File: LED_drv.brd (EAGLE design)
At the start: 160 x 100 mm, 42 parts, among them IC1 LM3409, IC2 LM393D, T1 IRLR9343PBF, T4 BT169, T5 BT169, T6 TLP266J

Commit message: Charge regeneration circuit
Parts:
- added C7: 1u/50V, rcl:C1206
- added D4: 5V1, diode:SOD80C
- added D6: 36V, diode:SOD80C
- added R22: 330R, resistor:R0805
- R10: value 33k -> 150k
- R11, R8, R9: value 33k -> 100k
- R12: value 33k -> 47k
- R13: value 33k -> 15k
- moved R13 305.7 mm to (-72.4, -251.5)
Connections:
- removed net V+: IC2.8
- removed net V-: IC2.4
- new net N$19: C7.1, D6.C, IC2.8, R13.1, R22.2
- new net N$20: IC2.3, R10.1, R11.1
- new net N$21: IC2.2, R8.2, R9.1
- new net N$22: D4.C, R11.2, R12.2
- new net N$27: R12.1, R22.1, R8.1
- new net N$29: IC2.1, R10.2, R13.2
- net GND: now also C7.2, D4.A, D6.A, IC2.4, IC2.5, IC2.6, IC2.7, R9.2
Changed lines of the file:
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@@
 <element name="L1" library="miscrel" package="CDRH104-R" value="CDRH104R" x="-36.83" y="8.89"/>
 <element name="R1" library="rcl" package="R0805" value="" x="-52.07" y="49.53"/>
-<element name="R10" library="resistor" package="R0805" value="33k" x="-54.61" y="44.45"/>
-<element name="R11" library="resistor" package="R0805" value="33k" x="-16.51" y="50.8"/>
-<element name="R12" library="resistor" package="R0805" value="33k" x="-21.59" y="50.8"/>
-<element name="R13" library="resistor" package="R0805" value="33k" x="-26.67" y="50.8"/>
+<element name="R10" library="resistor" package="R0805" value="150k" x="-54.61" y="44.45"/>
+<element name="R11" library="resistor" package="R0805" value="100k" x="-16.51" y="50.8"/>
+<element name="R12" library="resistor" package="R0805" value="47k" x="-21.59" y="50.8"/>
 <element name="R2" library="rcl" package="R0805" value="" x="-15.24" y="55.88"/>
 <element name="R3" library="rcl" package="R0805" value="1k" x="-46.99" y="50.8"/>
@@
 <element name="R6" library="pot" package="3RP/1610N" value="470k" x="-21.59" y="13.97"/>
 <element name="R7" library="rcl" package="R0805" value="15k" x="-31.75" y="50.8"/>
-<element name="R8" library="resistor" package="R0805" value="33k" x="-36.83" y="50.8"/>
-<element name="R9" library="resistor" package="R0805" value="33k" x="-41.91" y="50.8"/>
+<element name="R8" library="resistor" package="R0805" value="100k" x="-36.83" y="50.8"/>
+<element name="R9" library="resistor" package="R0805" value="100k" x="-41.91" y="50.8"/>
 <element name="S1" library="switch-omron" package="SW_DUMMY" value="SW_DUMMY" x="-20.32" y="55.88"/>
 <element name="T1" library="miscrel" package="TO252-3-11" value="IRLR9343PBF" x="-48.26" y="6.35"/>
@@
 <element name="R18" library="rcl" package="R1206" value="700R" x="-71.12" y="-212.09"/>
 <element name="C8" library="rcl" package="E3,5-8" value="100u" x="-69.85" y="-219.71"/>
+<element name="D4" library="diode" package="SOD80C" value="5V1" x="-71.12" y="-227.33"/>
+<element name="D6" library="diode" package="SOD80C" value="36V" x="-71.12" y="-232.41"/>
+<element name="R22" library="resistor" package="R0805" value="330R" x="-72.39" y="-237.49"/>
+<element name="C7" library="rcl" package="C1206" value="1u/50V" x="-69.85" y="-245.11"/>
+<element name="R13" library="resistor" package="R0805" value="15k" x="-72.39" y="-251.46"/>
 </elements>
 <signals>
-<signal name="V+">
-<contactref element="IC2" pad="8"/>
-</signal>
-<signal name="V-">
-<contactref element="IC2" pad="4"/>
-</signal>
 <signal name="N$1">
 <contactref element="R1" pad="2"/>
@@
 <contactref element="R6" pad="1"/>
 <contactref element="C5" pad="2"/>
-<wire x1="-21.59" y1="36.83" x2="-18.92" y2="44.45" width="0" layer="19" extent="1-1"/>
-<wire x1="-31.43" y1="44.45" x2="-21.59" y2="36.83" width="0" layer="19" extent="1-1"/>
-<wire x1="-36.83" y1="36.83" x2="-31.43" y2="44.45" width="0" layer="19" extent="1-1"/>
+<contactref element="R9" pad="2"/>
+<contactref element="IC2" pad="4"/>
+<contactref element="D4" pad="A"/>
+<contactref element="D6" pad="A"/>
+<contactref element="C7" pad="2"/>
+<contactref element="IC2" pad="6"/>
+<contactref element="IC2" pad="7"/>
+<contactref element="IC2" pad="5"/>
+<wire x1="-69.42" y1="-232.41" x2="-68.45" y2="-245.11" width="0" layer="19" extent="1-1"/>
+<wire x1="-69.42" y1="-227.33" x2="-69.42" y2="-232.41" width="0" layer="19" extent="1-1"/>
+<wire x1="-26.59" y1="13.97" x2="-69.42" y2="-227.33" width="0" layer="19" extent="1-1"/>
+<wire x1="-29.48" y1="24.27" x2="-26.59" y2="13.97" width="0" layer="19" extent="1-1"/>
+<wire x1="-30.48" y1="26.67" x2="-29.48" y2="24.27" width="0" layer="19" extent="1-1"/>
+<wire x1="-36.83" y1="36.83" x2="-30.48" y2="26.67" width="0" layer="19" extent="1-1"/>
 <wire x1="-44.94" y1="35.56" x2="-36.83" y2="36.83" width="0" layer="19" extent="1-1"/>
-<wire x1="-30.48" y1="26.67" x2="-36.83" y2="36.83" width="0" layer="19" extent="1-1"/>
-<wire x1="-29.48" y1="24.27" x2="-30.48" y2="26.67" width="0" layer="19" extent="1-1"/>
-<wire x1="-26.59" y1="13.97" x2="-29.48" y2="24.27" width="0" layer="19" extent="1-1"/>
-<wire x1="-53.02" y1="49.53" x2="-44.94" y2="35.56" width="0" layer="19" extent="1-1"/>
+<wire x1="-46.355" y1="28" x2="-44.94" y2="35.56" width="0" layer="19" extent="1-1"/>
+<wire x1="-47.625" y1="28" x2="-46.355" y2="28" width="0" layer="19" extent="1-1"/>
+<wire x1="-48.895" y1="28" x2="-47.625" y2="28" width="0" layer="19" extent="1-1"/>
+<wire x1="-46.355" y1="22.8" x2="-46.355" y2="28" width="0" layer="19" extent="1-1"/>
+<wire x1="-31.43" y1="44.45" x2="-36.83" y2="36.83" width="0" layer="19" extent="1-1"/>
+<wire x1="-40.96" y1="50.8" x2="-31.43" y2="44.45" width="0" layer="19" extent="1-1"/>
+<wire x1="-53.02" y1="49.53" x2="-40.96" y2="50.8" width="0" layer="19" extent="1-1"/>
+<wire x1="-21.59" y1="36.83" x2="-31.43" y2="44.45" width="0" layer="19" extent="1-1"/>
+<wire x1="-18.92" y1="44.45" x2="-21.59" y2="36.83" width="0" layer="19" extent="1-1"/>
 </signal>
 <signal name="N$4">
@@
 <wire x1="-70.77" y1="-197.62" x2="-69.698" y2="-212.09" width="0" layer="19" extent="1-1"/>
 </signal>
+<signal name="N$20">
+<contactref element="R10" pad="1"/>
+<contactref element="R11" pad="1"/>
+<contactref element="IC2" pad="3"/>
+<wire x1="-55.56" y1="44.45" x2="-17.46" y2="50.8" width="0" layer="19" extent="1-1"/>
+<wire x1="-47.625" y1="22.8" x2="-55.56" y2="44.45" width="0" layer="19" extent="1-1"/>
+</signal>
+<signal name="N$21">
+<contactref element="R8" pad="2"/>
+<contactref element="R9" pad="1"/>
+<contactref element="IC2" pad="2"/>
+<wire x1="-42.86" y1="50.8" x2="-48.895" y2="22.8" width="0" layer="19" extent="1-1"/>
+<wire x1="-35.88" y1="50.8" x2="-42.86" y2="50.8" width="0" layer="19" extent="1-1"/>
+</signal>
+<signal name="N$22">
+<contactref element="R11" pad="2"/>
+<contactref element="R12" pad="2"/>
+<contactref element="D4" pad="C"/>
+<wire x1="-20.64" y1="50.8" x2="-72.82" y2="-227.33" width="0" layer="19" extent="1-1"/>
+<wire x1="-15.56" y1="50.8" x2="-20.64" y2="50.8" width="0" layer="19" extent="1-1"/>
+</signal>
+<signal name="N$27">
+<contactref element="R12" pad="1"/>
+<contactref element="R8" pad="1"/>
+<contactref element="R22" pad="1"/>
+<wire x1="-37.78" y1="50.8" x2="-73.34" y2="-237.49" width="0" layer="19" extent="1-1"/>
+<wire x1="-22.54" y1="50.8" x2="-37.78" y2="50.8" width="0" layer="19" extent="1-1"/>
+</signal>
+<signal name="N$29">
+<contactref element="R10" pad="2"/>
+<contactref element="IC2" pad="1"/>
+<contactref element="R13" pad="2"/>
+<wire x1="-50.165" y1="22.8" x2="-71.44" y2="-251.46" width="0" layer="19" extent="1-1"/>
+<wire x1="-53.66" y1="44.45" x2="-50.165" y2="22.8" width="0" layer="19" extent="1-1"/>
+</signal>
+<signal name="N$19">
+<contactref element="IC2" pad="8"/>
+<contactref element="D6" pad="C"/>
+<contactref element="R22" pad="2"/>
+<contactref element="C7" pad="1"/>
+<contactref element="R13" pad="1"/>
+<wire x1="-71.25" y1="-245.11" x2="-73.34" y2="-251.46" width="0" layer="19" extent="1-1"/>
+<wire x1="-71.44" y1="-237.49" x2="-71.25" y2="-245.11" width="0" layer="19" extent="1-1"/>
+<wire x1="-72.82" y1="-232.41" x2="-71.44" y2="-237.49" width="0" layer="19" extent="1-1"/>
+<wire x1="-50.165" y1="28" x2="-72.82" y2="-232.41" width="0" layer="19" extent="1-1"/>
+</signal>
 </signals>

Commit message: Analog circuitry & switch correction
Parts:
- added C9: 100uF/50V, rcl:E3,5-8
- added D12: 1n4007, diode:DO-214AC
- added Q2: IRF840, transistor-fet:TO220
- added R23: 8M2, resistor:R0805
- added R25: 390R, resistor:R0805
- added R29: 330R, rcl:R1206
- added R30: 1M, rcl:R1206
- added T2: BC847, transistor:SOT23
- D5: value 1n4007 -> 18V; device diode:DO-214AC -> diode:SOD80C
- R14: value 330R/200V -> 2M
- R16: value 1M/200V -> 2M
- R17: value 1M/200V -> 47R; device rcl:R1206 -> resistor:R0805
- moved R17 366.0 mm to (-86.4, -401.3)
- moved R14 118.1 mm to (-71.1, -270.5)
- moved D5 104.1 mm to (-71.1, -264.2)
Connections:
- removed net N$24: B1.AC1, D9.A, R15.1, T4.2, T5.3
- new net 5V1_ZEN: D4.C, R11.2, R12.2, T2.1
- new net N$28: IC2.7, R17.1
- new net N$30: IC2.5, R17.2, R23.1, R25.2
- new net N$38: Q2.2, R29.1
- new net N$39: D12.A, Q2.3
- new net NAH: B1.AC2, D3.A, R19.2, R29.2, T4.3, T5.2
- new net V+: C9.+, R12.1, R22.1, R8.1, T6.1
- net 230VAC(L/N): now also B1.AC1; no longer D3.A, R19.2, T4.3, T5.2
- net 230VAC(N/L): now also D5.A, D9.A, R15.1, R30.1, T4.2, T5.3; no longer B1.AC2, R17.2
- net GND: now also C9.-, R23.2; no longer IC2.5, IC2.6, IC2.7
- net N$12: no longer R14.1
- net N$15: now also R14.1, R16.2; no longer D5.A, R14.2
- net N$16: now also D12.C; no longer D5.C
- net N$22: now also R25.1, T2.2; no longer D4.C, R11.2, R12.2
- net N$27: now also T2.3, T6.3; no longer R12.1, R22.1, R8.1
- net N$29: now also IC2.6
- net N$7: now also D5.C, Q2.1, R14.2, R30.2; no longer R16.2, R17.1

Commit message: Additional corrections
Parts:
- added R24: 2M2, resistor:R0805
- R23: value 8M2 -> 2M2
- T2: value BC847 -> (none); device transistor:SOT23 -> transistor:SOT89-BCE
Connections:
- new net N$21: IC2.5, R23.1, R24.1
- net 5V1_ZEN: now also T2.B; no longer T2.1
- net N$22: now also T2.E; no longer T2.2
- net N$27: now also T2.C; no longer T2.3
- net N$30: now also R24.2; no longer IC2.5, R23.1
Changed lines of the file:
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@@
 <element name="Q2" library="transistor-fet" package="TO220" value="IRF840" x="-83.82" y="-322.58"/>
 <element name="D12" library="diode" package="DO-214AC" value="1n4007" x="-85.09" y="-336.55"/>
-<element name="R23" library="resistor" package="R0805" value="8M2" x="-86.36" y="-367.03"/>
-<element name="T2" library="transistor" package="SOT23" value="BC847" x="-86.36" y="-381"/>
+<element name="R23" library="resistor" package="R0805" value="2M2" x="-86.36" y="-367.03"/>
+<element name="T2" library="transistor" package="SOT89-BCE" value="" x="-86.36" y="-381"/>
 <element name="R25" library="resistor" package="R0805" value="390R" x="-86.36" y="-394.97"/>
 <element name="R17" library="resistor" package="R0805" value="47R" x="-86.36" y="-401.32"/>
 <element name="C9" library="rcl" package="E3,5-8" value="100uF/50V" x="-83.82" y="-408.94"/>
+<element name="R24" library="resistor" package="R0805" value="2M2" x="-86.36" y="-416.56"/>
 </elements>
 <signals>
@@
 <contactref element="R12" pad="2"/>
 <contactref element="D4" pad="C"/>
-<contactref element="T2" pad="1"/>
-<wire x1="-72.82" y1="-227.33" x2="-87.31" y2="-382.1" width="0" layer="19" extent="1-1"/>
+<contactref element="T2" pad="B"/>
+<wire x1="-72.82" y1="-227.33" x2="-87.859" y2="-382.981" width="0" layer="19" extent="1-1"/>
 <wire x1="-20.64" y1="50.8" x2="-72.82" y2="-227.33" width="0" layer="19" extent="1-1"/>
 <wire x1="-15.56" y1="50.8" x2="-20.64" y2="50.8" width="0" layer="19" extent="1-1"/>
@@
 </signal>
 <signal name="N$30">
-<contactref element="R23" pad="1"/>
-<contactref element="IC2" pad="5"/>
 <contactref element="R25" pad="2"/>
 <contactref element="R17" pad="2"/>
+<contactref element="R24" pad="2"/>
+<wire x1="-85.41" y1="-401.32" x2="-85.41" y2="-416.56" width="0" layer="19" extent="1-1"/>
 <wire x1="-85.41" y1="-394.97" x2="-85.41" y2="-401.32" width="0" layer="19" extent="1-1"/>
-<wire x1="-87.31" y1="-367.03" x2="-85.41" y2="-394.97" width="0" layer="19" extent="1-1"/>
-<wire x1="-46.355" y1="28" x2="-87.31" y2="-367.03" width="0" layer="19" extent="1-1"/>
 </signal>
 <signal name="N$22">
-<contactref element="T2" pad="2"/>
+<contactref element="T2" pad="E"/>
 <contactref element="R25" pad="1"/>
-<wire x1="-85.41" y1="-382.1" x2="-87.31" y2="-394.97" width="0" layer="19" extent="1-1"/>
+<wire x1="-84.861" y1="-382.981" x2="-87.31" y2="-394.97" width="0" layer="19" extent="1-1"/>
 </signal>
 <signal name="N$27">
 <contactref element="T6" pad="3"/>
-<contactref element="T2" pad="3"/>
-<wire x1="-73" y1="-85.09" x2="-86.36" y2="-379.9" width="0" layer="19" extent="1-1"/>
+<contactref element="T2" pad="C"/>
+<wire x1="-73" y1="-85.09" x2="-86.36" y2="-382.727" width="0" layer="19" extent="1-1"/>
 </signal>
 <signal name="N$28">
@@
 <wire x1="-35.88" y1="50.8" x2="-42.86" y2="50.8" width="0" layer="19" extent="1-1"/>
 </signal>
+<signal name="N$21">
+<contactref element="R23" pad="1"/>
+<contactref element="IC2" pad="5"/>
+<contactref element="R24" pad="1"/>
+<wire x1="-87.31" y1="-367.03" x2="-87.31" y2="-416.56" width="0" layer="19" extent="1-1"/>
+<wire x1="-46.355" y1="28" x2="-87.31" y2="-367.03" width="0" layer="19" extent="1-1"/>
+</signal>
 </signals>

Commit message: Mains side PCB layout
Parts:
- removed B1: (no value), rectifier:FBP1,5
- removed C8: 100u, rcl:E3,5-8
- removed D12: 1n4007, diode:DO-214AC
- added D7: 1n4007, diode:DO-214AC
- added D8: 10V, diode:SOD80C
- added PAD1, PAD2, PAD3, PAD4: (no value), wirepad:SMD2,54-5,08
- added R26: 10M, rcl:R1206
- Q2: value IRF840 -> IPD50R380; device transistor-fet:TO220 -> miscrel:TO252-3-11
- R18: value 700R -> 10M
- T2: value (none) -> BCX56; device transistor:SOT89-BCE -> miscrel:SOT89
- moved R25 479.5 mm to (-20.3, 80.0)
- moved C9 475.8 mm to (-39.4, 64.8)
- moved T2 453.3 mm to (-11.4, 66.0)
- moved R24 446.6 mm to (-14.0, 24.1)
- moved R17 436.4 mm to (-15.2, 29.2)
- moved R23 394.0 mm to (-7.62, 19.1)
- moved R29 392.9 mm to (62.2, 47.0), turned to 90 degrees
- moved Q2 390.3 mm to (55.9, 41.9), turned to 90 degrees
- moved R30 387.0 mm to (64.1, 33.7), turned to 90 degrees
- moved R14 336.4 mm to (62.9, 38.1), turned to 180 degrees
- moved D5 326.0 mm to (61.6, 33.7), turned to 270 degrees
- moved R18 290.5 mm to (72.5, 40.4), turned to 180 degrees
- moved R13 288.2 mm to (-12.7, 30.5)
- moved D4 275.8 mm to (-11.4, 41.9)
- moved D6 274.3 mm to (-12.7, 35.6)
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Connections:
- removed net N$17: B1.+, C8.+, R18.1
- removed net N$18: B1.-, C8.-, R18.2
- new net N$24: D7.C, R29.2
- new net N$33: D8.C, Q2.3
- net 230VAC(L/N): now also PAD1.1, PAD4.1; no longer B1.AC1
- net 230VAC(N/L): now also PAD2.1, R26.2, T4.4
- net N$14: now also R18.1
- net N$16: now also R21.2, T6.4; no longer D12.C, D9.C, R15.2, R21.1, T5.1
- net N$25: now also R20.2; no longer R21.2
- net N$26: now also R18.2, R26.1; no longer R20.2, T6.4
- net N$27: now also T2.C@1
- net N$39: now also D8.A, D9.C, R15.2, R21.1, T5.1; no longer D12.A, Q2.3
- net NAH: now also D7.A, PAD3.1, T5.4; no longer B1.AC2, R29.2
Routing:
- net 230VAC(N/L): track 0.00 -> 76.3 mm
- net NAH: track 0.00 -> 47.4 mm
- net N$39: track 0.00 -> 16.6 mm
- net N$23: track 0.00 -> 15.0 mm
- net N$7: track 0.00 -> 7.31 mm
- net N$33: track 0.00 -> 5.82 mm
- net N$24: track 0.00 -> 3.50 mm
- net N$26: track 0.00 -> 3.35 mm
- net N$15: track 0.00 -> 3.06 mm
- net N$38: track 0.00 -> 2.81 mm
- net 230VAC(L/N): track 0.00 -> 2.79 mm
- net N$16: track 0.00 -> 1.99 mm
- net N$25: track 0.00 -> 1.78 mm

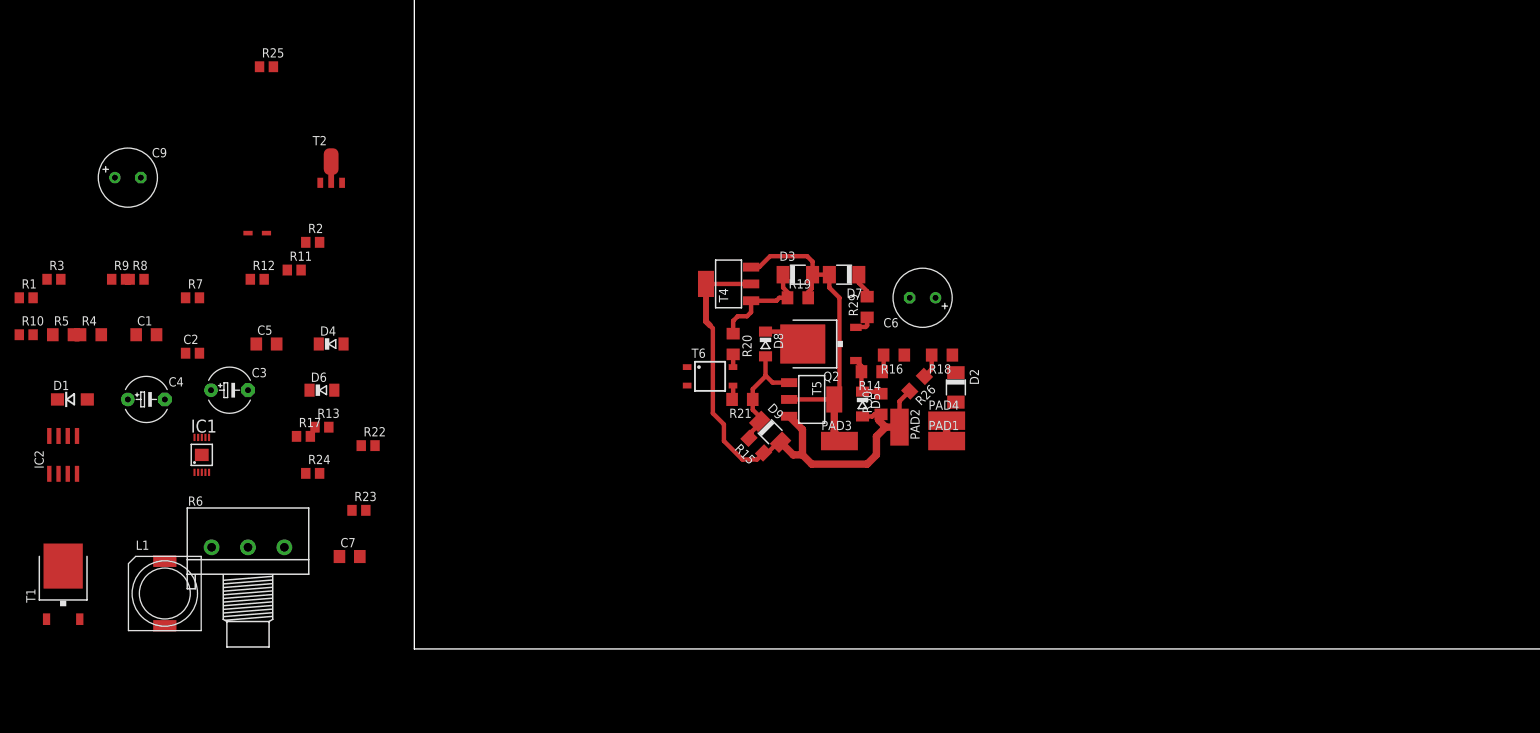
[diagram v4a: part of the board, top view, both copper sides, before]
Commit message: key side PCB layout
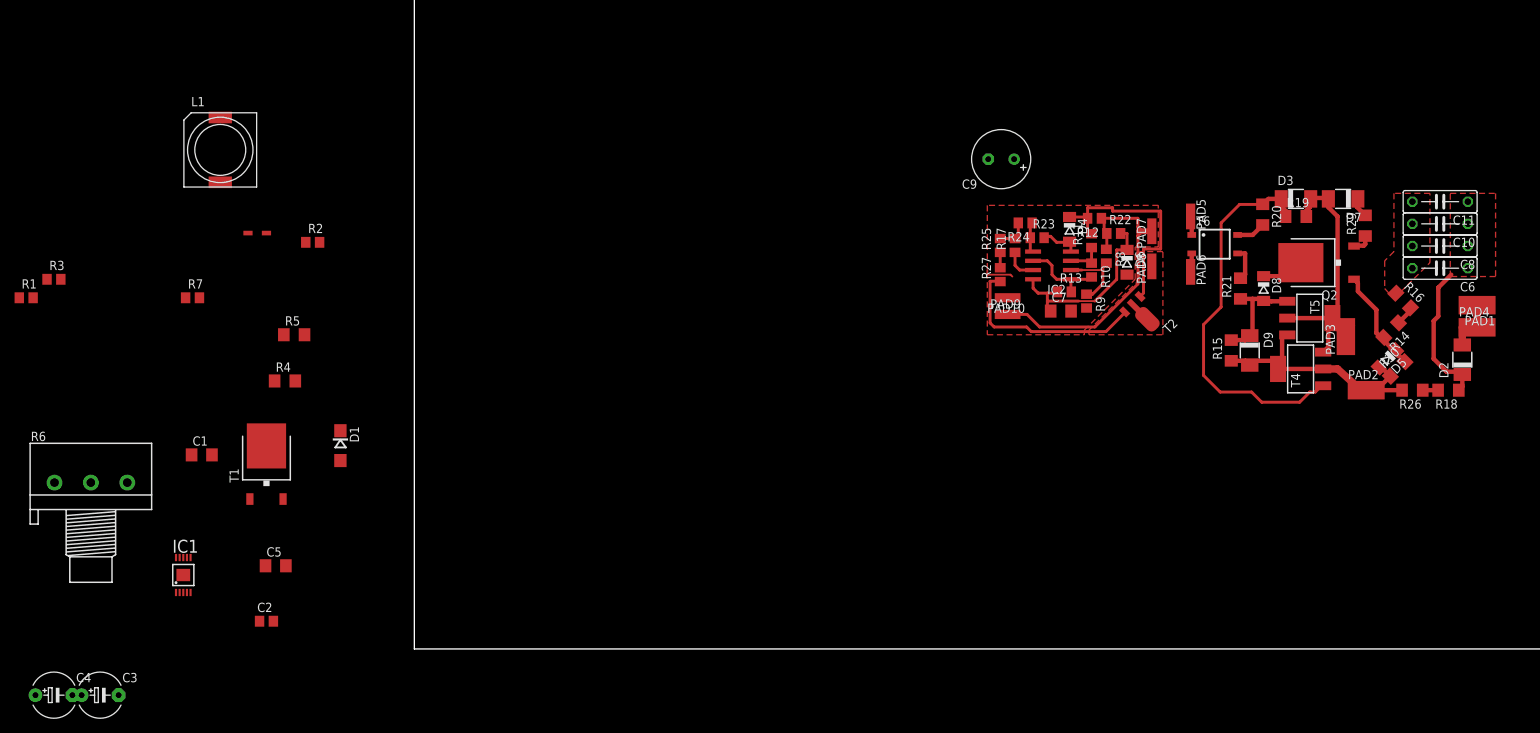
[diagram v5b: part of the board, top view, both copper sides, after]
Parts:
- added C10, C11, C8: 100n/400V, rcl:C075-032X103
- added PAD10, PAD5, PAD6, PAD7, PAD8, PAD9: (no value), wirepad:SMD1,27-2,54
- added R27: 0, resistor:R0805
- C6: device rcl:E3,5-8 -> rcl:C075-032X103
- moved R10 146.7 mm to (93.1, 52.1), turned to 270 degrees
- moved IC2 138.4 mm to (87.6, 52.7), turned to 90 degrees
- moved R8 133.2 mm to (95.1, 54.0), turned to 270 degrees
- moved R9 133.1 mm to (92.4, 47.8), turned to 270 degrees
- moved C9 120.0 mm to (80.6, 67.3), turned to 180 degrees
- moved R12 115.4 mm to (93.5, 59.2), turned to 180 degrees
- moved T2 113.3 mm to (100.1, 46.0), turned to 225 degrees
- moved D6 112.0 mm to (97.9, 53.1), turned to 270 degrees
- moved R11 109.6 mm to (93.1, 56.1), turned to 90 degrees
- moved R22 106.5 mm to (96.1, 57.1)
- moved R24 103.8 mm to (83.9, 58.5), turned to 180 degrees
- moved R25 103.8 mm to (80.5, 55.4), turned to 90 degrees
- moved R13 103.7 mm to (89.3, 49.1)
- moved C7 103.4 mm to (88.8, 46.4)
- moved D4 102.7 mm to (90.0, 57.7), turned to 270 degrees
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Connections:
- new net N$34: C10.2, C11.2, C6.2, C8.2, R16.1
- net GND: now also PAD10.1
- net N$12: now also R25.1, R27.2; no longer C6.-, R16.1
- net N$14: now also C10.1, C11.1, C6.1, C8.1; no longer C6.+
- net N$22: now also R27.1; no longer R25.1
- net N$27: now also PAD6.1, PAD8.1
- net V+: now also PAD5.1, PAD7.1, PAD9.1
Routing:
- net V+: track 0.00 -> 45.2 mm
- net 230VAC(N/L): track 76.3 -> 36.4 mm
- net N$23: track 15.0 -> 53.3 mm
- net 5V1_ZEN: track 0.00 -> 31.6 mm
- net N$22: track 0.00 -> 27.3 mm
- net N$31: track 0.00 -> 27.1 mm
- net N$14: track 0.00 -> 19.8 mm
- net N$29: track 0.00 -> 11.7 mm
- net N$19: track 0.00 -> 10.3 mm
- net GND: track 0.00 -> 9.66 mm
- net N$7: track 7.31 -> 14.9 mm
- net NAH: track 47.4 -> 41.1 mm
- net N$20: track 0.00 -> 5.29 mm
- net 230VAC(L/N): track 2.79 -> 7.50 mm
- net N$28: track 0.00 -> 4.54 mm
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- added copper zone on layer 1, net GND
- added copper zone on layer 1, net N$14
- added copper zone on layer 1, net N$27
- added copper zone on layer 1, net N$34
